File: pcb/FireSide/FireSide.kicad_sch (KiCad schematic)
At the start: 27 parts, among them J0 SDIOModule, J1 D4184_PIN_A, J10 5V_01x02_JST, J11 5V_01x02_JST, J12 Status_01x02_JST, J2 D4184_PIN_B, J3 D4184_PIN_C, J4 A0_01x02_JST, J5 A1_01x02_JST, J6 A2_01x02_JST, J60 XT60-Male, J7 A3_01x02_JST, J8 A4_01x02_JST, J9 A5_01x02_JST, Q1 MMBT2222A, U1 AMS1117-5.0, U3 RYLR998

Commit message: [FS] PCB Updated to v1.1.6
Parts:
- removed A1: Nucleo-L412KB, Module:Arduino_Nano, symbol MCU_Module:Arduino_Nano_Every
- removed C1, C2: 22u, Capacitor_THT:CP_Radial_D5.0mm_P2.50mm, symbol Device:C_Polarized
- removed H5, H6: BoardM4, MountingHole:MountingHole_4.3mm_M4_ISO7380_Pad_TopBottom, symbol Mechanical:MountingHole_Pad
- removed J0: SDIOModule, Connector_Molex:Molex_Nano-Fit_105309-xx08_1x08_P2.50mm_Vertical, symbol Connector_Generic:Conn_01x08
- removed J1: D4184_PIN_A, Connector_JST:JST_XH_B4B-XH-A_1x04_P2.50mm_Vertical, symbol Connector:Conn_01x04_Pin
- removed J2: D4184_PIN_B, Connector_JST:JST_XH_B4B-XH-A_1x04_P2.50mm_Vertical, symbol Connector:Conn_01x04_Pin
- removed J3: D4184_PIN_C, Connector_JST:JST_XH_B4B-XH-A_1x04_P2.50mm_Vertical, symbol Connector:Conn_01x04_Pin
- removed J60: XT60-Male, XT60-M:AMASS_XT60-M, symbol XT60-M:XT60-M
- removed J9: A5_01x02_JST, Connector_JST:JST_XH_B2B-XH-A_1x02_P2.50mm_Vertical, symbol Connector:Conn_01x02_Pin
- removed R1: 1k, Resistor_SMD:R_0805_2012Metric_Pad1.20x1.40mm_HandSolder, symbol Device:R
- removed U1: AMS1117-5.0, Package_TO_SOT_SMD:SOT-223-3_TabPin2, symbol Regulator_Linear:AMS1117-5.0
- removed U3: RYLR998, RYLR998:RYLR998, symbol RYLR998:RYLR998
- added C1, C4: 22uF, Capacitor_SMD:C_0805_2012Metric, symbol Device:C
- added C2, C3: 10uF, Capacitor_SMD:C_0805_2012Metric, symbol Device:C
- added C5: 100nF, Capacitor_SMD:C_0805_2012Metric, symbol Device:C
- added C6: 4.7uF, Capacitor_SMD:C_0805_2012Metric, symbol Device:C
- added J1, J14, J2: Conn_01x02_Pin, Connector_JST:JST_XH_B2B-XH-A_1x02_P2.50mm_Vertical, symbol Connector:Conn_01x02_Pin
- added J13, J9: Screw_Terminal_01x03, TerminalBlock:TerminalBlock_bornier-3_P5.08mm, symbol Connector:Screw_Terminal_01x03
- added J3: Conn_01x08_Pin, Connector_PinHeader_2.54mm:PinHeader_1x08_P2.54mm_Vertical, symbol Connector:Conn_01x08_Pin
- added R2, R5, R6, R7: 100k, Resistor_THT:R_Axial_DIN0204_L3.6mm_D1.6mm_P5.08mm_Horizontal, symbol Device:R
- added R4: 1k, Resistor_SMD:R_0805_2012Metric, symbol Device:R
- added TP1, TP2: TestPoint, TestPoint:TestPoint_Loop_D2.60mm_Drill1.6mm_Beaded, symbol Connector:TestPoint
- added U1: AMS1117-3.3, Package_TO_SOT_SMD:SOT-223-3_TabPin2, symbol Regulator_Linear:AMS1117-3.3
- added U2: ~, FireSide Footprint:RYLR998, symbol FireSide symbol:RYLR998
- added U3: NUCLEO-L412KB, FireSide Footprint:NUCLEO-L412KB, symbol FireSide symbol:NUCLEO-L412KB
- added U4: AMS1117-5.0, Package_TO_SOT_SMD:SOT-223-3_TabPin2, symbol Regulator_Linear:AMS1117-5.0
- added U5, U6, U9: ~, FireSide Footprint:D4184, symbol FireSide symbol:D4184
- added U8: ~, FireSide Footprint:XT60-M, symbol FireSide symbol:XT60-M
- H1, H2: value SDModuleM3 -> MountingHole_Pad; footprint MountingHole:MountingHole_3.2mm_M3_ISO7380_Pad_TopBottom -> MountingHole:MountingHole_4.3mm_M4_DIN965_Pad
- H3, H4: value BoardM4 -> MountingHole_Pad; footprint MountingHole:MountingHole_4.3mm_M4_ISO7380_Pad_TopBottom -> MountingHole:MountingHole_4.3mm_M4_DIN965_Pad
- J10, J11: value 5V_01x02_JST -> Conn_01x02_Pin
- J12: value Status_01x02_JST -> Conn_01x02_Pin
- J4: value A0_01x02_JST -> Conn_01x02_Pin
- J5: value A1_01x02_JST -> Conn_01x02_Pin
- J6: value A2_01x02_JST -> Conn_01x02_Pin
- J7: value A3_01x02_JST -> Conn_01x02_Pin
- J8: value A4_01x02_JST -> Conn_01x02_Pin
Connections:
- net +BATT is gone; now on net GND: J12.1 (Pin_1)
- net GND: now also J11.1 (Pin_1), J7.1 (Pin_1), J8.1 (Pin_1), C1.2, C2.2, C3.2, C4.2, C5.2, C6.2, J1.2 (Pin_2), J13.2 (Pin_2), J14.2 (Pin_2), J2.2 (Pin_2), J3.2 (Pin_2), J9.2 (Pin_2), U1.1 (GND), U2.5 (GND), U3.CN3_4 (GND_CN3), U4.1 (GND), U5.1 (GND), U6.1 (GND), U8.N (NEG), U9.1 (GND); no longer J10.2 (Pin_2), J11.2 (Pin_2), J7.2 (Pin_2), J8.2 (Pin_2)
- net STATUS_PIN: now also U3.CN3_8 (PB6/D5)
- net A_THERM-2: now reaches J5.1 (Pin_1)
- net A_THERM-2: now also R5.2, U3.CN4_9 (PA4/A3)
- net 3.3V: now reaches J12.2 (Pin_2)
- net 3.3V: now also J11.2 (Pin_2), C4.1, J9.1 (Pin_1), TP2.1, U1.2 (VO)
- net at Q1.3 (C): now also R4.1
- net A_THERM-1: now reaches J4.1 (Pin_1)
- net A_THERM-1: now also R2.2, U3.CN4_10 (PA3/A2)
- net A_THERM-3: now reaches J6.1 (Pin_1)
- net A_THERM-3: now also R6.2, U3.CN4_8 (PA5/A4)
- net 5VIN: no longer names the net of J10.1 (Pin_1)
- net 5VIN: now also R4.2; no longer J11.1 (Pin_1)
- new net 3.3V_STM: J3.1 (Pin_1), R2.1, R5.1, R6.1, R7.1, U3.CN4_14 (+3V3)
- new net 3.3Vin: J9.3 (Pin_3), U2.1 (VDD)
- new net 5V: C1.1, J13.3 (Pin_3), J7.2 (Pin_2), J8.2 (Pin_2), TP1.1, U4.2 (VO)
- new net 5Vin: C5.1, C6.1, J13.1 (Pin_1), U3.CN4_1 (VIN)
- new net A0: J1.1 (Pin_1), U3.CN4_12 (PA0/A0)
- new net A1: J2.1 (Pin_1), U3.CN4_11 (PA1/A1)
- new net A_THERM-4: J14.1 (Pin_1), R7.2, U3.CN4_7 (PA6/A5)
- new net CS_SD: J3.6 (Pin_6), U3.CN3_13 (PA11/D10)
- new net MISO_SD: J3.4 (Pin_4), U3.CN3_15 (PB4/D12)
- new net MOSI_SD: J3.5 (Pin_5), U3.CN3_14 (PB5/D11)
- new net PWM_D4184-1: U3.CN3_6 (PB0/D3), U5.2 (PWM)
- new net PWM_D4184-2: U3.CN3_9 (PB1/D6), U9.2 (PWM)
- new net PWM_D4184-3: U3.CN3_12 (PA8/D9), U6.2 (PWM)
- new net RX_RYLR: U2.3 (RXD), U3.CN3_1 (PA9/D1)
- new net SCK_SD: J3.3 (Pin_3), U3.CN4_15 (PB3/D13)
- new net TX_RYLR: U2.4 (TXD), U3.CN3_2 (PA10/D0)
- new net VI: C2.1, C3.1, J10.2 (Pin_2), U1.3 (VI), U4.3 (VI), U8.P (POS)
- no-connect marks 12 -> 23
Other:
- note added: "100K THERMISTORS"
- note added: "3.3V"
- note added: "5V"
- note added: "ANALOG CHANNELS"
- note added: "D4184 (1)"
- note added: "D4184 (2)"
- note added: "D4184 (3)"
- note added: "IGNITION W/ D4184"
- note added: "MCU SWITCH"
- note added: "MOUNTING HOLES"
- note added: "NUCLEO-L412KB"
- note added: "POWER CHANNELS"
- note added: "POWER SUPPLY (3.3V)"
- note added: "POWER SUPPLY (5V)"
- note added: "RYLR SWITCH"
- note added: "RYLR998"
- note added: "SD CARD READER"
- note added: "STATUS INDICATOR CIRCUIT"
- note added: "TEST POINTS"
- note added: "THERMISTOR (1)"
- note added: "THERMISTOR (2)"
- note added: "THERMISTOR (3)"
- note added: "THERMISTOR (4)"
- note removed: "Regulated 5V Domain"
- note removed: "Status Indicator Circuit"
- title: FireSide -> FireSide v2.0

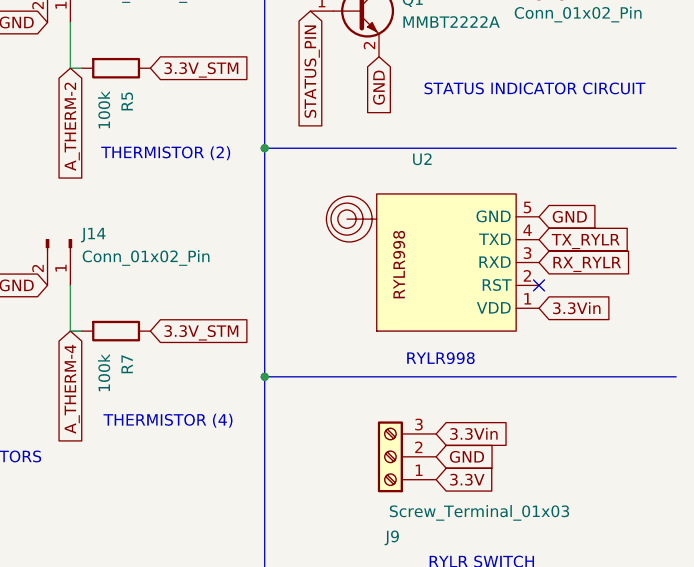
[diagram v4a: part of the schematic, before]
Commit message: [FS] Updated FireSide PCB with RYLR993
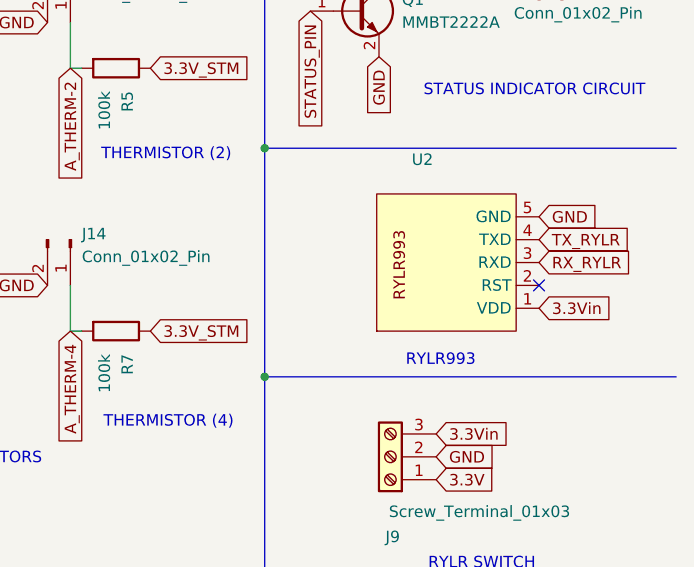
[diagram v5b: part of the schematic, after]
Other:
- note added: "RYLR993"
- note removed: "RYLR998"
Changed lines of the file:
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@@
 		)
 	)
-	(text "RYLR998\n"
+	(text "RYLR993\n"
 		(exclude_from_sim no)
 		(at 260.858 99.822 0)

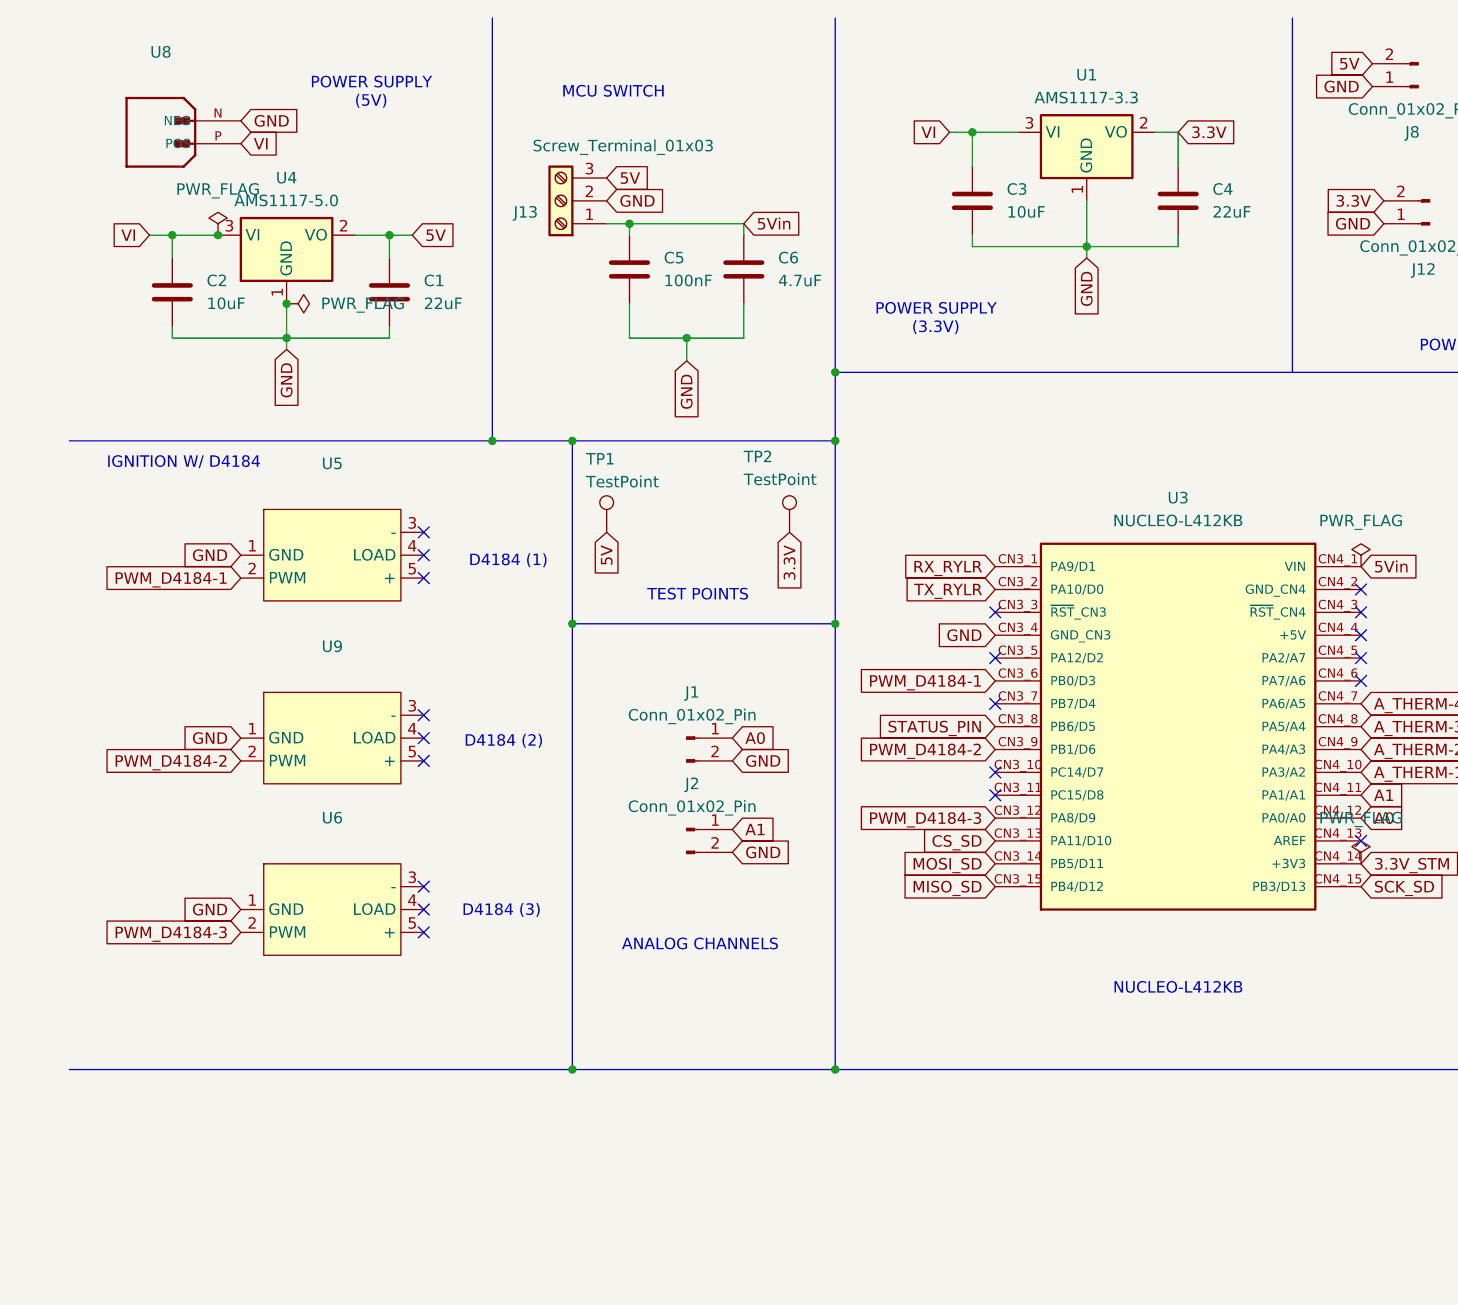
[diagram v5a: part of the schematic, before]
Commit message: [FS] Updated PCB (v1.2.0)
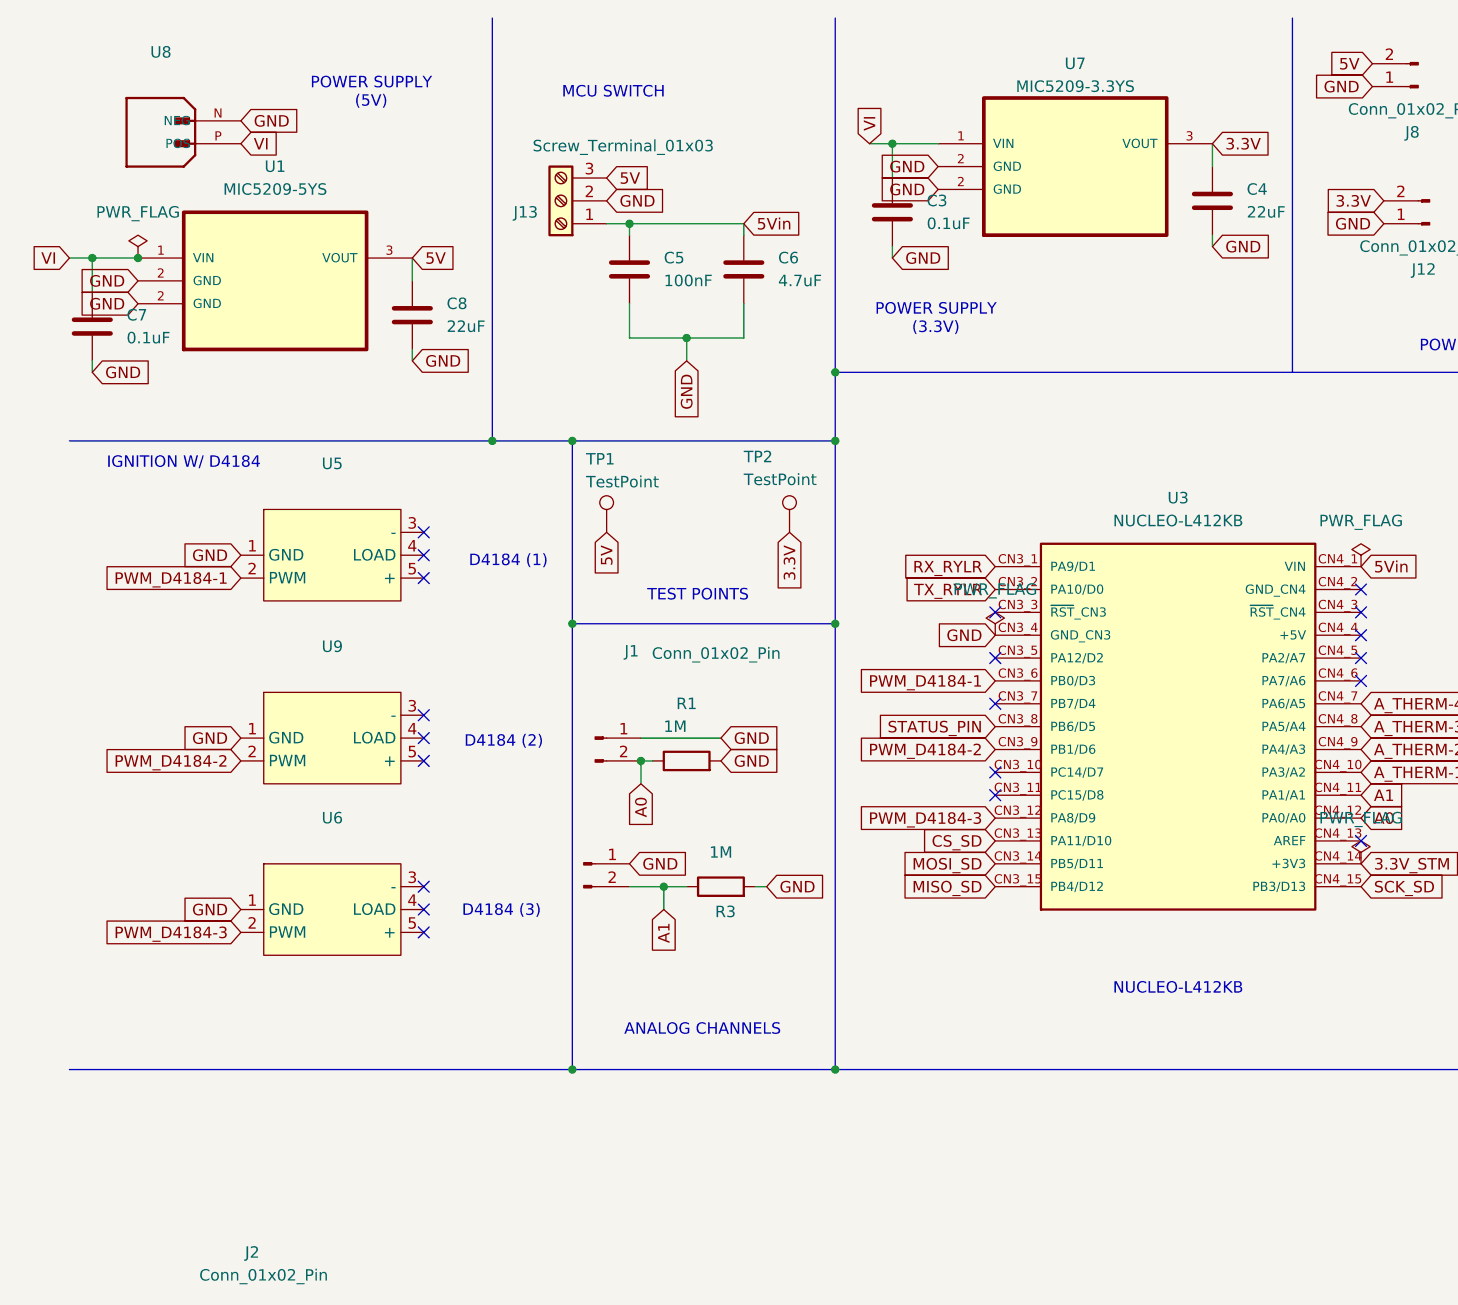
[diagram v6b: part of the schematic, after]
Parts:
- removed C1: 22uF, Capacitor_SMD:C_0805_2012Metric, symbol Device:C
- removed C2: 10uF, Capacitor_SMD:C_0805_2012Metric, symbol Device:C
- removed U1: AMS1117-3.3, Package_TO_SOT_SMD:SOT-223-3_TabPin2, symbol Regulator_Linear:AMS1117-3.3
- removed U4: AMS1117-5.0, Package_TO_SOT_SMD:SOT-223-3_TabPin2, symbol Regulator_Linear:AMS1117-5.0
- added C7: 0.1uF, Capacitor_SMD:C_0805_2012Metric, symbol Device:C
- added C8: 22uF, Capacitor_SMD:C_0805_2012Metric, symbol Device:C
- added R1, R3: 1M, Resistor_THT:R_Axial_DIN0204_L3.6mm_D1.6mm_P5.08mm_Horizontal, symbol Device:R
- added U1: MIC5209-5YS, MIC5209-5.0YS-TR:SOT230P700X180-4N, symbol mic5209-3.3ys:MIC5209-3.3YS
- added U7: MIC5209-3.3YS, MIC5209-3.3YS-Microchip-Symbol-Kicad-237169:SOT-223-3, symbol mic5209-3.3ys:MIC5209-3.3YS
- C3: value 10uF -> 0.1uF
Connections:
- net 3.3V: now also U7.3 (VOUT)
- net 5V: now also C8.1, U1.3 (VOUT)
- net A0: now also J1.2 (Pin_2), R1.1; no longer J1.1 (Pin_1)
- net A1: now also J2.2 (Pin_2), R3.1; no longer J2.1 (Pin_1)
- net GND: now also J1.1 (Pin_1), J2.1 (Pin_1), C7.2, C8.2, R1.2, R3.2, U1.2 (GND), U7.2 (GND); no longer J1.2 (Pin_2), J2.2 (Pin_2)
- net VI: now also C7.1, U1.1 (VIN), U7.1 (VIN)
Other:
- moved on the sheet: C3, C4, J1, J2

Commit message: [FS] Remove AMS1117 Regulators & Apply ECSS-E-ST-20-21C Standard
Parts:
- C5: value 100nF -> 0.1uF
- J13, J9: footprint TerminalBlock:TerminalBlock_bornier-3_P5.08mm -> TerminalBlock:TerminalBlock_MaiXu_MX126-5.0-03P_1x03_P5.00mm
- R2, R5, R6, R7: value 100k -> 100k +/- 0.1%; footprint Resistor_THT:R_Axial_DIN0204_L3.6mm_D1.6mm_P5.08mm_Horizontal -> Resistor_SMD:R_0805_2012Metric
- U1: footprint MIC5209-5.0YS-TR:SOT230P700X180-4N -> Package_TO_SOT_SMD:SOT-223-3_TabPin2; symbol mic5209-3.3ys:MIC5209-3.3YS -> FireSide symbol:MIC5209
- U2: footprint FireSide Footprint:RYLR998 -> FireSide Footprint:RYLR993; symbol FireSide symbol:RYLR998 -> FireSide symbol:RYLR993
- U7: footprint MIC5209-3.3YS-Microchip-Symbol-Kicad-237169:SOT-223-3 -> Package_TO_SOT_SMD:SOT-223-3_TabPin2; symbol mic5209-3.3ys:MIC5209-3.3YS -> FireSide symbol:MIC5209
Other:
- title: FireSide v2.0 -> FireSide
- moved on the sheet: C3, C4, C7, C8, J14, J2, J4, J6, R1, R2, R6, R7
